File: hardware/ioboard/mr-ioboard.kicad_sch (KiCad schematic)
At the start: 146 parts, among them J1 Conn_01x40_Shielded, J2 USB_C_Receptacle_USB2.0, J3 Conn_01x06, J4 Micro_SD_Card_Det, J5 Conn_01x04, J6 Conn_01x02, Q1 2N7002, SW1 SW_Push, SW2 SW_Push, SW3 SW_Push, SW4 SW_Push, SW5 SW_Push, U1 AP3402, U10 F1C200S, U11 AP64501, U2 AP64501, U3 TPD2E2U06, U4 DS90C363, U5 TPD2E2U06, U6 LD3985M28R_SOT23, U7 AP3402, U8 FUSB302BMPX, U9 TPD2E2U06, Y1 24MHz

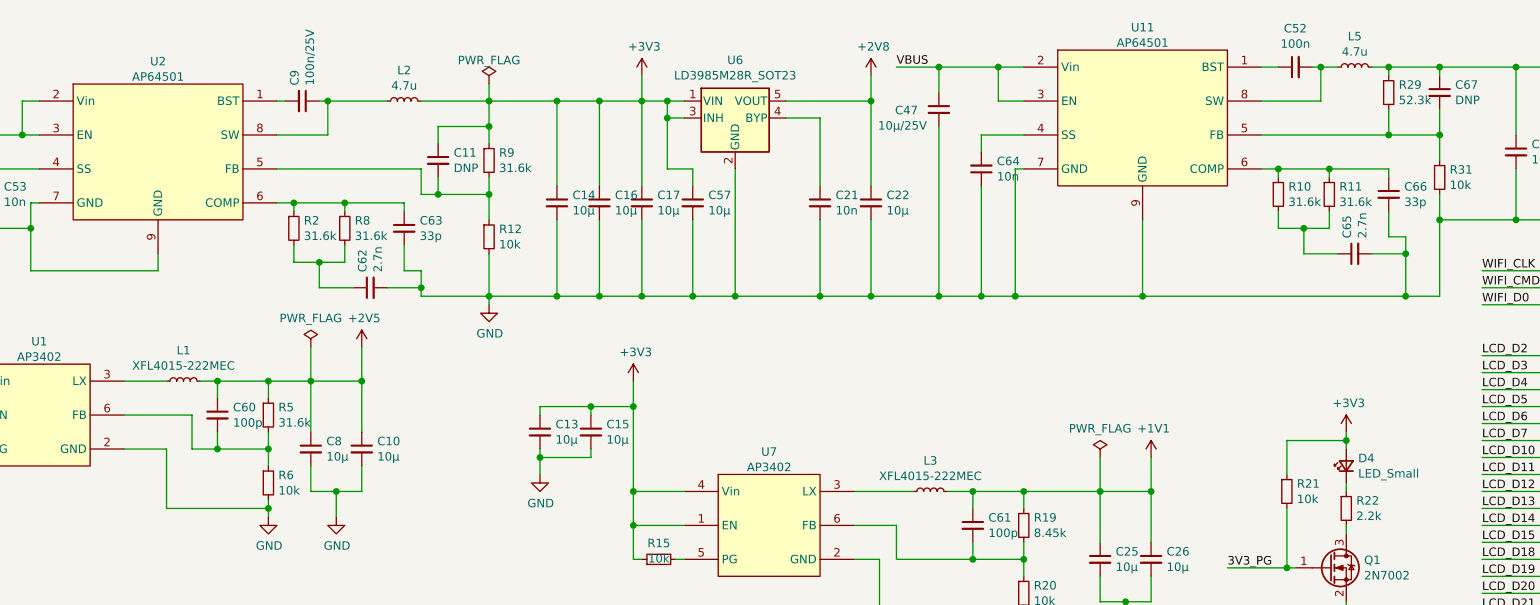
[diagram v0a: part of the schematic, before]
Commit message: Update some inductor part numbers
Signed-off-by: gatecat <gatecat@ds0.me>
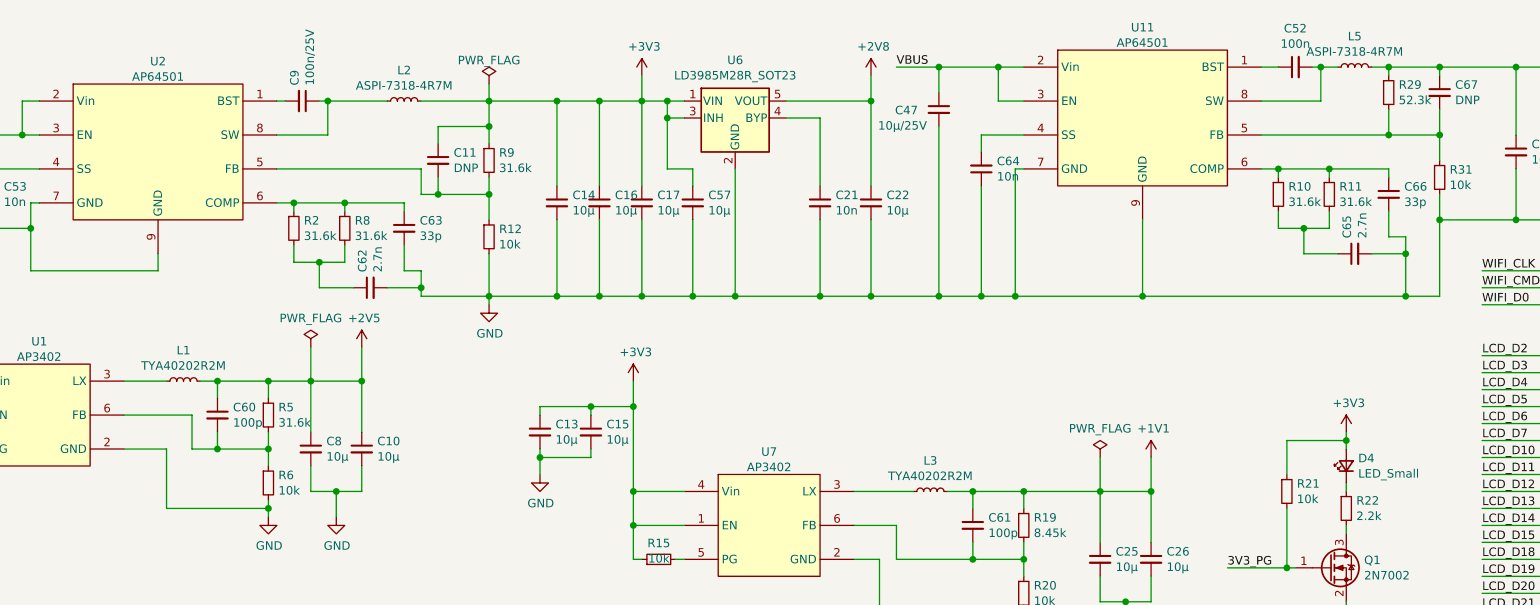
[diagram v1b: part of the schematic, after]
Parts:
- L1, L3: value XFL4015-222MEC -> TYA40202R2M; footprint Inductor_SMD:L_Coilcraft_XxL4020 -> Inductor_SMD:L_Taiyo-Yuden_NR-40xx
- L2, L5: value 4.7u -> ASPI-7318-4R7M
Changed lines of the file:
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@@
     (in_bom yes) (on_board yes)
     (property "Reference" "L1" (id 0) (at 80.01 61.4488 90))
-    (property "Value" "XFL4015-222MEC" (id 1) (at 80.01 63.747 90))
-    (property "Footprint" "Inductor_SMD:L_Coilcraft_XxL4020" (id 2) (at 80.01 66.04 0)
+    (property "Value" "TYA40202R2M" (id 1) (at 80.01 63.747 90))
+    (property "Footprint" "Inductor_SMD:L_Taiyo-Yuden_NR-40xx" (id 2) (at 80.01 66.04 0)
       (effects (font (size 1.27 1.27)) hide)
     )
@@
     (in_bom yes) (on_board yes)
     (property "Reference" "L2" (id 0) (at 113.03 19.5388 90))
-    (property "Value" "4.7u" (id 1) (at 113.03 21.838 90))
+    (property "Value" "ASPI-7318-4R7M" (id 1) (at 113.03 21.838 90))
     (property "Footprint" "Inductor_SMD:L_Bourns_SRP7028A_7.3x6.6mm" (id 2) (at 113.03 24.13 0)
       (effects (font (size 1.27 1.27)) hide)
@@
     (in_bom yes) (on_board yes)
     (property "Reference" "L3" (id 0) (at 191.77 77.9588 90))
-    (property "Value" "XFL4015-222MEC" (id 1) (at 191.77 80.257 90))
-    (property "Footprint" "Inductor_SMD:L_Coilcraft_XxL4020" (id 2) (at 191.77 82.55 0)
+    (property "Value" "TYA40202R2M" (id 1) (at 191.77 80.257 90))
+    (property "Footprint" "Inductor_SMD:L_Taiyo-Yuden_NR-40xx" (id 2) (at 191.77 82.55 0)
       (effects (font (size 1.27 1.27)) hide)
     )
@@
     (in_bom yes) (on_board yes)
     (property "Reference" "L5" (id 0) (at 255.27 14.4588 90))
-    (property "Value" "4.7u" (id 1) (at 255.27 16.758 90))
+    (property "Value" "ASPI-7318-4R7M" (id 1) (at 255.27 16.758 90))
     (property "Footprint" "Inductor_SMD:L_Bourns_SRP7028A_7.3x6.6mm" (id 2) (at 255.27 19.05 0)
       (effects (font (size 1.27 1.27)) hide)
@@
     )
     (path "/7cba76ed-5206-4c88-b6e5-8a7d65fa4357"
-      (reference "L1") (unit 1) (value "XFL4015-222MEC") (footprint "Inductor_SMD:L_Coilcraft_XxL4020")
+      (reference "L1") (unit 1) (value "TYA40202R2M") (footprint "Inductor_SMD:L_Taiyo-Yuden_NR-40xx")
     )
     (path "/c272eb0b-582e-4a43-9683-d3e011ab888f"
-      (reference "L2") (unit 1) (value "4.7u") (footprint "Inductor_SMD:L_Bourns_SRP7028A_7.3x6.6mm")
+      (reference "L2") (unit 1) (value "ASPI-7318-4R7M") (footprint "Inductor_SMD:L_Bourns_SRP7028A_7.3x6.6mm")
     )
     (path "/12b10813-9f8e-43a1-a184-90e944538aca"
-      (reference "L3") (unit 1) (value "XFL4015-222MEC") (footprint "Inductor_SMD:L_Coilcraft_XxL4020")
+      (reference "L3") (unit 1) (value "TYA40202R2M") (footprint "Inductor_SMD:L_Taiyo-Yuden_NR-40xx")
     )
     (path "/40d017ba-b962-4f34-93cc-40feddf8e09a"
@@
     )
     (path "/f90a4892-bfac-4e27-b9b5-55224167ff6b"
-      (reference "L5") (unit 1) (value "4.7u") (footprint "Inductor_SMD:L_Bourns_SRP7028A_7.3x6.6mm")
+      (reference "L5") (unit 1) (value "ASPI-7318-4R7M") (footprint "Inductor_SMD:L_Bourns_SRP7028A_7.3x6.6mm")
     )
     (path "/bf767ab0-d986-441b-9076-8f9d5f44d287"
